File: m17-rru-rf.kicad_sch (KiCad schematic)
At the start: 0 parts

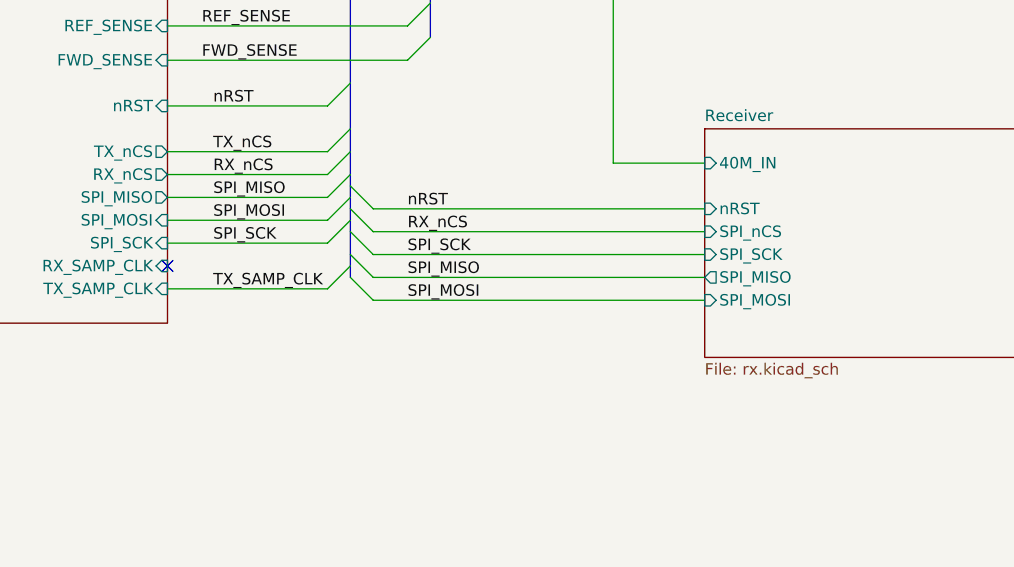
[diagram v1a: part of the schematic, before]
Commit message: WIP rev B
- added bleed resistors
- power supply now uses linear regulators
- routed RX_SAMP_CLK
- added some decoupling at RF_PA_VDD
- added some GND vias here and there
- updated BOM
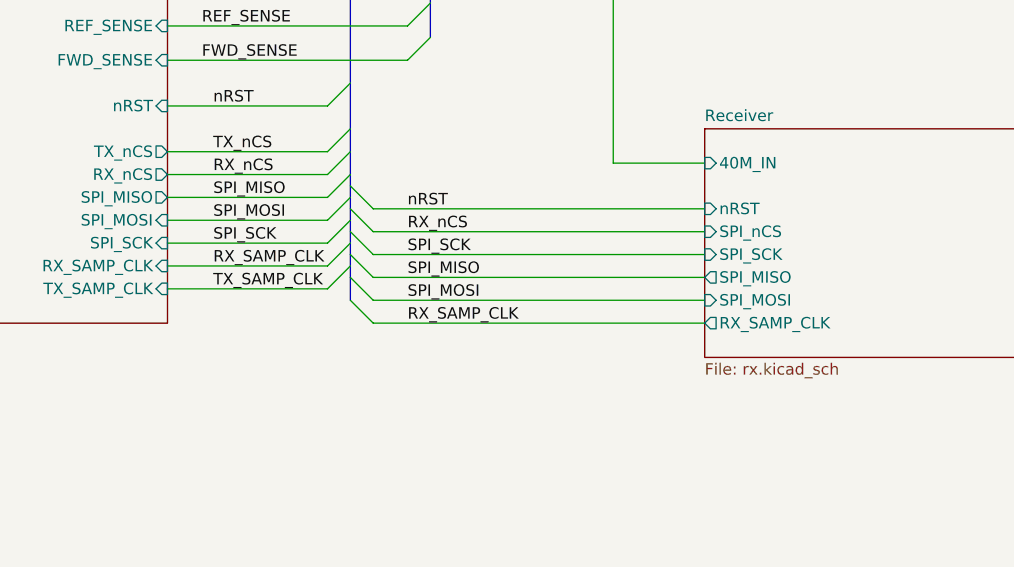
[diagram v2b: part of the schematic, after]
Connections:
- no-connect marks 1 -> 0
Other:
- sheet Receiver ports: added RX_SAMP_CLK; removed none
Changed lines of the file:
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@@
   (title_block
     (title "Remote Radio Unit - RF board")
-    (date "18-01-2024")
+    (date "19-01-2024")
     (rev "B")
     (company "M17 Project")
     (comment 1 "Wojciech Kaczmarski, SP5WWP")
   )
-  (bus_alias "CTRL_BUS" (members "SPI_MISO" "SPI_MOSI" "SPI_SCK" "TX_nCS" "RX_nCS" "nRST" "TX_SAMP_CLK"))
+  (bus_alias "CTRL_BUS" (members "SPI_MISO" "SPI_MOSI" "SPI_SCK" "TX_nCS" "RX_nCS" "nRST" "TX_SAMP_CLK" "RX_SAMP_CLK"))
   (bus_alias "RF_SENSE_BUS" (members "REF_SENSE" "FWD_SENSE"))
   (junction (at 134.62 184.15) (diameter 0) (color 0 0 0 0)
@@
   (junction (at 198.12 184.15) (diameter 0) (color 0 0 0 0)
   )
-  (no_connect (at 80.01 218.44))
   (bus_entry (at 109.22 193.04) (size -2.54 2.54)
     (stroke (width 0) (type default))
@@
     (stroke (width 0) (type default))
   )
+  (bus_entry (at 100.33 222.25) (size 2.54 2.54)
+    (stroke (width 0) (type default))
+  )
   (bus_entry (at 100.33 205.74) (size -2.54 2.54)
     (stroke (width 0) (type default))
@@
     (stroke (width 0) (type default))
   )
+  (bus_entry (at 100.33 215.9) (size -2.54 2.54)
+    (stroke (width 0) (type default))
+  )
   (bus_entry (at 100.33 217.17) (size 2.54 2.54)
     (stroke (width 0) (type default))
@@
     (stroke (width 0) (type default))
   )
+  (wire (pts (xy 80.01 218.44) (xy 97.79 218.44))
+    (stroke (width 0) (type default))
+  )
   (wire (pts (xy 102.87 69.85) (xy 139.7 69.85))
     (stroke (width 0) (type default))
@@
     (stroke (width 0) (type default))
   )
+  (bus (pts (xy 100.33 219.71) (xy 100.33 222.25))
+    (stroke (width 0) (type default))
+  )
   (wire (pts (xy 102.87 74.93) (xy 139.7 74.93))
     (stroke (width 0) (type default))
@@
     (stroke (width 0) (type default))
   )
+  (wire (pts (xy 102.87 224.79) (xy 139.7 224.79))
+    (stroke (width 0) (type default))
+  )
   (bus (pts (xy 100.33 210.82) (xy 100.33 212.09))
     (stroke (width 0) (type default))
   )
-  (bus (pts (xy 100.33 214.63) (xy 100.33 217.17))
+  (bus (pts (xy 100.33 214.63) (xy 100.33 215.9))
     (stroke (width 0) (type default))
   )
@@
   )
   (bus (pts (xy 312.42 133.35) (xy 312.42 139.7))
+    (stroke (width 0) (type default))
+  )
+  (bus (pts (xy 100.33 215.9) (xy 100.33 217.17))
     (stroke (width 0) (type default))
   )
@@
     (effects (font (size 1.27 1.27)) (justify left bottom))
   )
+  (label "RX_SAMP_CLK" (at 85.09 218.44 0)
+    (effects (font (size 1.27 1.27)) (justify left bottom))
+  )
   (label "REF_SENSE" (at 83.82 127 0) (fields_autoplaced)
     (effects (font (size 1.27 1.27)) (justify left bottom))
@@
   )
   (label "SPI_MISO" (at 83.82 114.3 0) (fields_autoplaced)
+    (effects (font (size 1.27 1.27)) (justify left bottom))
+  )
+  (label "RX_SAMP_CLK" (at 106.68 224.79 0)
     (effects (font (size 1.27 1.27)) (justify left bottom))
   )
@@
       (effects (font (size 1.27 1.27)) (justify left))
     )
+    (pin "RX_SAMP_CLK" output (at 139.7 224.79 180)
+      (effects (font (size 1.27 1.27)) (justify left))
+    )

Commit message: WIP rev C
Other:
- sheet Exciter ports: added none; removed 40M_OUT
- sheet Receiver ports: added none; removed 40M_IN
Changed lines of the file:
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@@
   (title_block
     (title "Remote Radio Unit - RF board")
-    (date "20-01-2024")
-    (rev "B")
+    (date "04-04-2024")
+    (rev "C")
     (company "M17 Project")
     (comment 1 "Wojciech Kaczmarski, SP5WWP")
@@
     (stroke (width 0) (type default))
   )
-  (wire (pts (xy 139.7 82.55) (xy 129.54 82.55))
-    (stroke (width 0) (type default))
-  )
   (wire (pts (xy 134.62 85.09) (xy 134.62 184.15))
     (stroke (width 0) (type default))
@@
     (stroke (width 0) (type default))
   )
-  (wire (pts (xy 129.54 82.55) (xy 129.54 207.01))
-    (stroke (width 0) (type default))
-  )
   (wire (pts (xy 80.01 213.36) (xy 97.79 213.36))
     (stroke (width 0) (type default))
@@
   )
   (wire (pts (xy 198.12 184.15) (xy 198.12 207.01))
-    (stroke (width 0) (type default))
-  )
-  (wire (pts (xy 129.54 207.01) (xy 139.7 207.01))
     (stroke (width 0) (type default))
   )
@@
       (effects (font (size 1.27 1.27)) (justify right))
     )
-    (pin "40M_IN" input (at 139.7 207.01 180)
-      (effects (font (size 1.27 1.27)) (justify left))
-    )
     (pin "RX_SAMP_CLK" output (at 139.7 224.79 180)
       (effects (font (size 1.27 1.27)) (justify left))
@@
       (effects (font (size 1.27 1.27)) (justify left))
     )
-    (pin "40M_OUT" output (at 139.7 82.55 180)
-      (effects (font (size 1.27 1.27)) (justify left))
-    )
